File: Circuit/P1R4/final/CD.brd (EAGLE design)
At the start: 59.7 x 59.7 mm, 127 parts, among them U1 MK20DX256VLH7, U2 TPS61200, U3 MPU-9250, Y1 32.768KHz, Y2 16Mhz/8pF, Y3 26 Mhz, Y4 16 Mhz

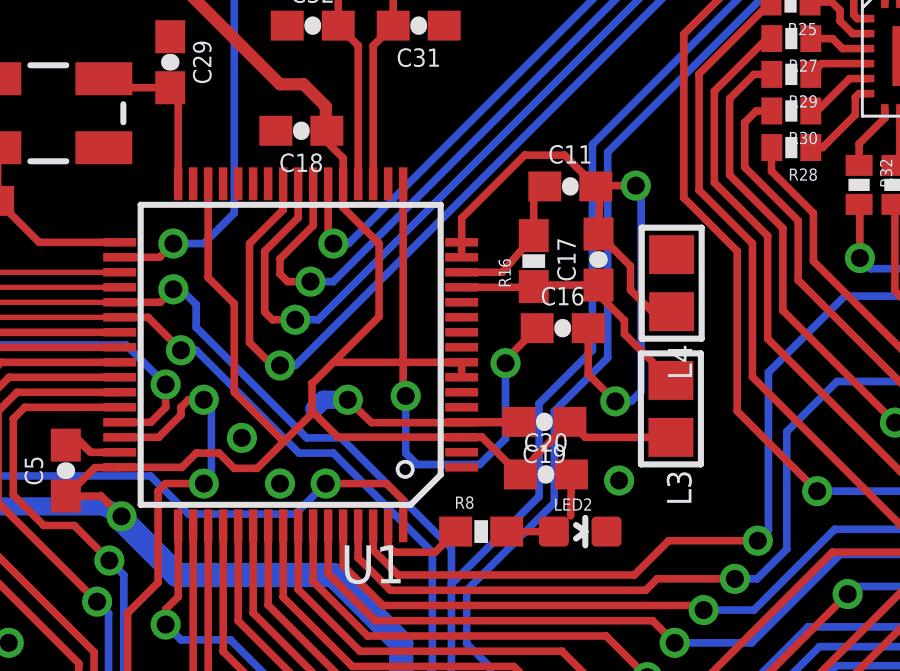
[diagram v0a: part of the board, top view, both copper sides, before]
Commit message: Overlap fixed on R4. Preliminary R3 complete
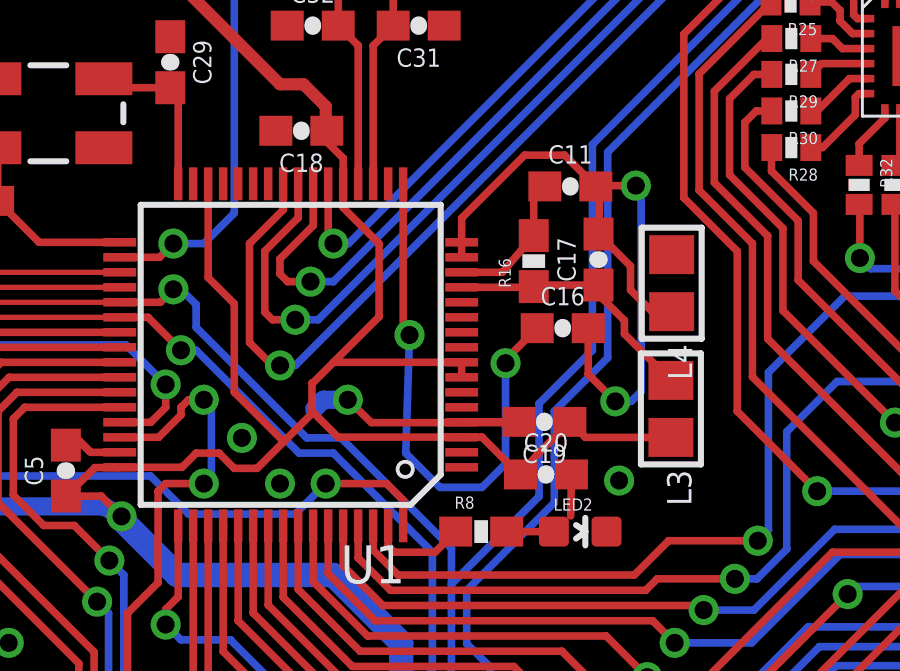
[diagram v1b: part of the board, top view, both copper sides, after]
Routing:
- net VREF_OUT: track 17.0 -> 18.2 mm
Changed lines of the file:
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@@
 <wire x1="36.6404" y1="35.1536" x2="35.5854" y2="34.0986" width="0.254" layer="1"/>
 <wire x1="35.5854" y1="34.0986" x2="35.5854" y2="33.9852" width="0.254" layer="1"/>
-<wire x1="34.7218" y1="30.607" x2="35.5854" y2="31.4706" width="0.254" layer="16"/>
-<wire x1="35.5854" y1="31.4706" x2="35.5854" y2="33.9852" width="0.254" layer="16"/>
-<wire x1="34.7218" y1="30.607" x2="32.639" y2="30.607" width="0.254" layer="16"/>
-<wire x1="32.1726" y1="39.9646" x2="32.1726" y2="32.9784" width="0.254" layer="1"/>
-<wire x1="32.1726" y1="32.9784" x2="32.258" y2="32.893" width="0.254" layer="1"/>
-<via x="32.258" y="32.893" extent="1-16" drill="0.6"/>
-<wire x1="32.258" y1="32.893" x2="32.258" y2="30.988" width="0.254" layer="16"/>
-<wire x1="32.258" y1="30.988" x2="32.639" y2="30.607" width="0.254" layer="16"/>
+<wire x1="35.5854" y1="31.4706" x2="35.5854" y2="31.877" width="0.254" layer="16"/>
+<wire x1="35.5854" y1="31.877" x2="35.5854" y2="33.9852" width="0.254" layer="16"/>
+<wire x1="32.1726" y1="39.9646" x2="32.1726" y2="35.1374" width="0.254" layer="1"/>
+<wire x1="32.1726" y1="35.1374" x2="32.385" y2="34.925" width="0.254" layer="1"/>
+<via x="32.385" y="34.925" extent="1-16" drill="0.6"/>
+<wire x1="32.385" y1="34.925" x2="32.258" y2="30.988" width="0.254" layer="16"/>
+<wire x1="32.258" y1="30.988" x2="33.401" y2="29.845" width="0.254" layer="16"/>
+<wire x1="33.401" y1="29.845" x2="34.798" y2="29.845" width="0.254" layer="16"/>
+<wire x1="34.798" y1="29.845" x2="35.5854" y2="30.6324" width="0.254" layer="16"/>
+<wire x1="35.5854" y1="30.6324" x2="35.5854" y2="31.4706" width="0.254" layer="16"/>
 </signal>
 <signal name="N$27">
